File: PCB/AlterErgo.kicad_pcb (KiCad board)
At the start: 2 copper layers, 97 parts, among them J1 GS3, J2 SJ-43514, J3 GS3, SW0:10 SW_Push, SW0:11 SW_Push, SW0:12 SW_Push, SW0:7 SW_Push, SW0:8 SW_Push, SW0:9 SW_Push, SW1 SW_SPST, SW1:10 SW_Push, SW1:11 SW_Push, SW1:12 SW_Push, SW1:13 SW_Push, SW1:9 SW_Push, SW2:10 SW_Push, SW2:11 SW_Push, SW2:12 SW_Push, SW2:13 SW_Push, SW2:7 SW_Push, SW2:8 SW_Push, SW2:9 SW_Push, SW3:10 SW_Push, SW3:11 SW_Push, SW3:12 SW_Push, SW3:13 SW_Push, SW3:8 SW_Push, SW3:9 SW_Push, SW4:10 SW_Push, SW4:11 SW_Push, SW4:12 SW_Push, SW4:13 SW_Push, SW4:7 SW_Push, SW4:8 SW_Push, SW4:9 SW_Push, SW5:10 SW_Push, SW5:11 SW_Push, SW5:12 SW_Push, SW5:13 SW_Push, SW5:7 SW_Push, SW5:8 SW_Push, SW5:9 SW_Push, U1 Feather32u4Bluefruit, U2 MCP23018

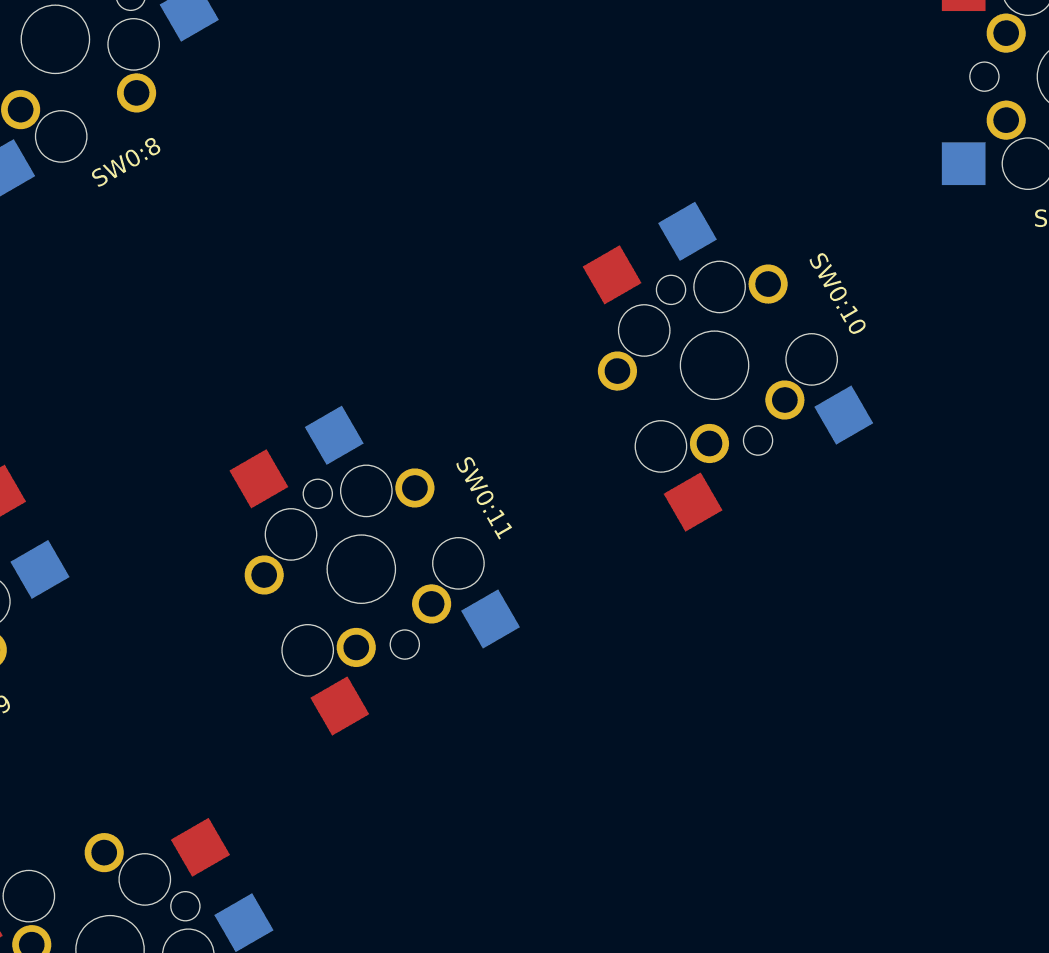
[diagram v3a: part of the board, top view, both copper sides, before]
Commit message: Add stabilizer mounting holes to 2U keys in thumb cluster
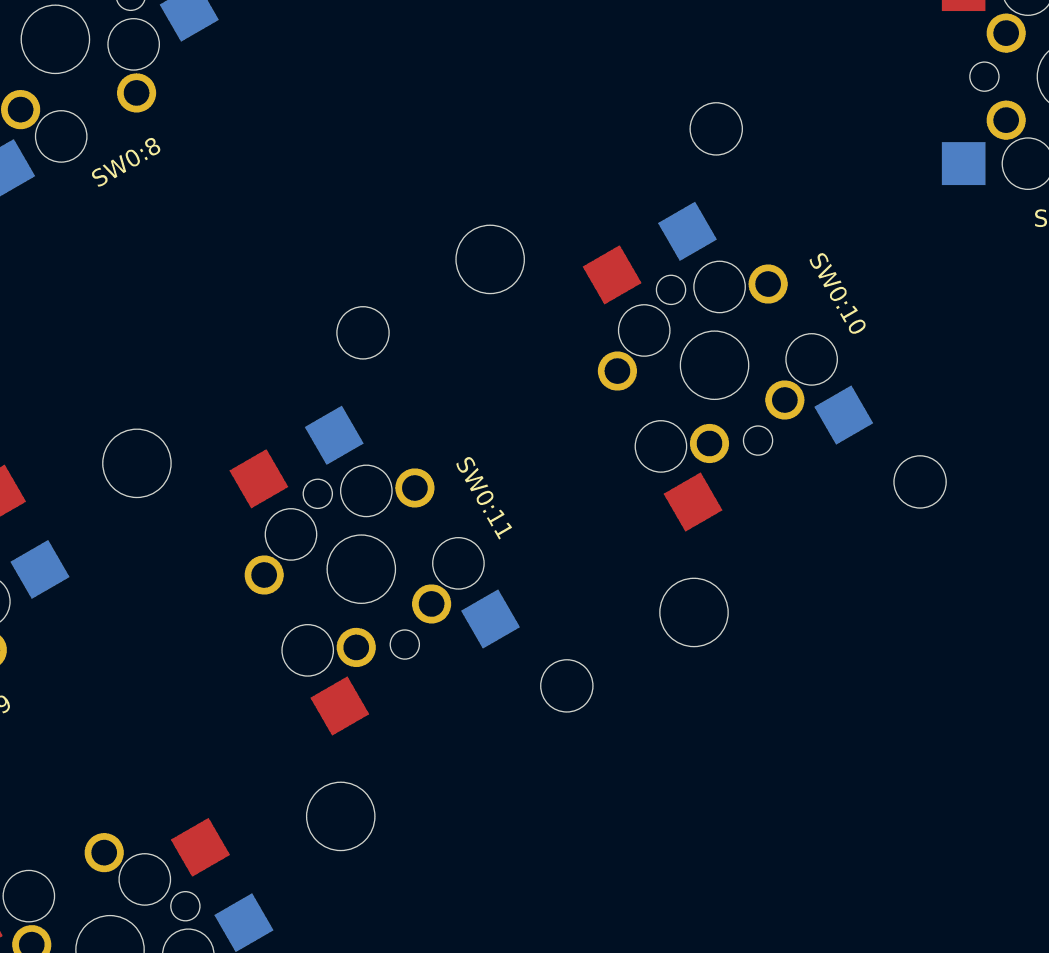
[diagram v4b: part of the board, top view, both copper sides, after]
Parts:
- added SW0:10: SW_Push, keyswitches:Kailh_socket_optional_reversible, F.Cu at (110.1, 168.7)
- added Stab0:11: SW_Stabilizer, keyswitches:MX_Stabilizer_2u, F.Cu at (89.5, 180.6)
- Stab0:10: renamed from SW0:10; value SW_Push -> SW_Stabilizer; footprint keyswitches:Kailh_socket_optional_reversible -> keyswitches:MX_Stabilizer_2u
- turned Stab0:10 to 300 degrees
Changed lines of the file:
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@@
     (links 388)
     (no_connects 388)
-    (area 40.508856 -74.833 449.550001 213.296599)
+    (area 40.556456 -74.7854 449.502401 213.248999)
     (thickness 1.6)
     (drawings 11)
     (tracks 0)
     (zones 0)
-    (modules 97)
+    (modules 99)
     (nets 83)
   )
@@
   )
   (module keyswitches:Kailh_socket_optional_reversible (layer F.Cu)
+    (at 110.132883 168.652792 120)
+    (descr "MX-style keyswitch with support for reversible optional Kailh socket")
+    (tags MX,cherry,gateron,kailh,pg1511,socket)
+    (fp_text reference SW0:10 (at 0 8.3 120) (layer F.SilkS)
+      (effects (font (size 1 1) (thickness 0.15)))
+    )
+    (fp_text value SW_Push (at 0 -8.7 120) (layer F.Fab)
+      (effects (font (size 1 1) (thickness 0.15)))
+    )
+    (fp_line (start -7 -6) (end -7 -7) (layer B.SilkS) (width 0.15))
+    (fp_line (start -7 -7) (end -6 -7) (layer B.SilkS) (width 0.15))
+    (fp_line (start -6 7) (end -7 7) (layer B.SilkS) (width 0.15))
+    (fp_line (start -7 7) (end -7 6) (layer B.SilkS) (width 0.15))
+    (fp_line (start 7 6) (end 7 7) (layer B.SilkS) (width 0.15))
+    (fp_line (start 7 7) (end 6 7) (layer B.SilkS) (width 0.15))
+    (fp_line (start 6 -7) (end 7 -7) (layer B.SilkS) (width 0.15))
+    (fp_line (start 7 -7) (end 7 -6) (layer B.SilkS) (width 0.15))
+    (fp_line (start -6.9 6.9) (end 6.9 6.9) (layer Eco2.User) (width 0.15))
+    (fp_line (start 6.9 -6.9) (end -6.9 -6.9) (layer Eco2.User) (width 0.15))
+    (fp_line (start 6.9 -6.9) (end 6.9 6.9) (layer Eco2.User) (width 0.15))
+    (fp_line (start -6.9 6.9) (end -6.9 -6.9) (layer Eco2.User) (width 0.15))
+    (fp_line (start -7.5 -7.5) (end 7.5 -7.5) (layer Eco2.User) (width 0.15))
+    (fp_line (start 7.5 -7.5) (end 7.5 7.5) (layer Eco2.User) (width 0.15))
+    (fp_line (start 7.5 7.5) (end -7.5 7.5) (layer Eco2.User) (width 0.15))
+    (fp_line (start -7.5 7.5) (end -7.5 -7.5) (layer Eco2.User) (width 0.15))
+    (pad 1 smd rect (at -6.29 5.08 120) (size 2.55 2.5) (layers B.Cu B.Paste B.Mask)
+      (net 60 /ROW0))
+    (pad 2 smd rect (at 7.56 2.54 120) (size 2.55 2.5) (layers B.Cu B.Paste B.Mask)
+      (net 8 "Net-(D0:10-Pad2)"))
+    (pad "" np_thru_hole circle (at -2.54 -5.08 120) (size 3 3) (drill 3) (layers *.Cu *.Mask))
+    (pad "" np_thru_hole circle (at 3.81 -2.54 120) (size 3 3) (drill 3) (layers *.Cu *.Mask))
+    (pad 2 thru_hole circle (at 2.54 5.08 120) (size 2.286 2.286) (drill 1.4986) (layers *.Cu *.Mask)
+      (net 8 "Net-(D0:10-Pad2)"))
+    (pad 1 thru_hole circle (at -3.81 2.54 120) (size 2.286 2.286) (drill 1.4986) (layers *.Cu *.Mask)
+      (net 60 /ROW0))
+    (pad 1 smd rect (at -6.29 -5.08 120) (size 2.55 2.5) (layers F.Cu F.Paste F.Mask)
+      (net 60 /ROW0))
+    (pad "" np_thru_hole circle (at -2.54 5.08 120) (size 3 3) (drill 3) (layers *.Cu *.Mask))
+    (pad "" np_thru_hole circle (at 3.81 2.54 120) (size 3 3) (drill 3) (layers *.Cu *.Mask))
+    (pad 2 thru_hole circle (at 2.54 -5.08 120) (size 2.286 2.286) (drill 1.4986) (layers *.Cu *.Mask)
+      (net 8 "Net-(D0:10-Pad2)"))
+    (pad "" np_thru_hole circle (at 0 0 120) (size 3.9878 3.9878) (drill 3.9878) (layers *.Cu *.Mask))
+    (pad 1 thru_hole circle (at -3.81 -2.54 120) (size 2.286 2.286) (drill 1.4986) (layers *.Cu *.Mask)
+      (net 60 /ROW0))
+    (pad "" np_thru_hole circle (at 5.08 0 120) (size 1.7018 1.7018) (drill 1.7018) (layers *.Cu *.Mask))
+    (pad "" np_thru_hole circle (at -5.08 0 120) (size 1.7018 1.7018) (drill 1.7018) (layers *.Cu *.Mask))
+    (pad 2 smd rect (at 7.56 -2.54 120) (size 2.55 2.5) (layers F.Cu F.Paste F.Mask)
+      (net 8 "Net-(D0:10-Pad2)"))
+  )
+  (module keyswitches:Kailh_socket_optional_reversible (layer F.Cu)
     (at 107.15628 107.1563)
     (descr "MX-style keyswitch with support for reversible optional Kailh socket")
@@
   )
   (module keyswitches:Kailh_socket_optional_reversible (layer F.Cu)
-    (at 110.132883 168.652792 120)
-    (descr "MX-style keyswitch with support for reversible optional Kailh socket")
-    (tags MX,cherry,gateron,kailh,pg1511,socket)
-    (fp_text reference SW0:10 (at 0 8.3 120) (layer F.SilkS)
-      (effects (font (size 1 1) (thickness 0.15)))
-    )
-    (fp_text value SW_Push (at 0 -8.7 120) (layer F.Fab)
-      (effects (font (size 1 1) (thickness 0.15)))
-    )
-    (fp_line (start -7 -6) (end -7 -7) (layer B.SilkS) (width 0.15))
-    (fp_line (start -7 -7) (end -6 -7) (layer B.SilkS) (width 0.15))
-    (fp_line (start -6 7) (end -7 7) (layer B.SilkS) (width 0.15))
-    (fp_line (start -7 7) (end -7 6) (layer B.SilkS) (width 0.15))
-    (fp_line (start 7 6) (end 7 7) (layer B.SilkS) (width 0.15))
-    (fp_line (start 7 7) (end 6 7) (layer B.SilkS) (width 0.15))
-    (fp_line (start 6 -7) (end 7 -7) (layer B.SilkS) (width 0.15))
-    (fp_line (start 7 -7) (end 7 -6) (layer B.SilkS) (width 0.15))
-    (fp_line (start -6.9 6.9) (end 6.9 6.9) (layer Eco2.User) (width 0.15))
-    (fp_line (start 6.9 -6.9) (end -6.9 -6.9) (layer Eco2.User) (width 0.15))
-    (fp_line (start 6.9 -6.9) (end 6.9 6.9) (layer Eco2.User) (width 0.15))
-    (fp_line (start -6.9 6.9) (end -6.9 -6.9) (layer Eco2.User) (width 0.15))
-    (fp_line (start -7.5 -7.5) (end 7.5 -7.5) (layer Eco2.User) (width 0.15))
-    (fp_line (start 7.5 -7.5) (end 7.5 7.5) (layer Eco2.User) (width 0.15))
-    (fp_line (start 7.5 7.5) (end -7.5 7.5) (layer Eco2.User) (width 0.15))
-    (fp_line (start -7.5 7.5) (end -7.5 -7.5) (layer Eco2.User) (width 0.15))
-    (pad 1 smd rect (at -6.29 5.08 120) (size 2.55 2.5) (layers B.Cu B.Paste B.Mask)
-      (net 60 /ROW0))
-    (pad 2 smd rect (at 7.56 2.54 120) (size 2.55 2.5) (layers B.Cu B.Paste B.Mask)
-      (net 8 "Net-(D0:10-Pad2)"))
-    (pad "" np_thru_hole circle (at -2.54 -5.08 120) (size 3 3) (drill 3) (layers *.Cu *.Mask))
-    (pad "" np_thru_hole circle (at 3.81 -2.54 120) (size 3 3) (drill 3) (layers *.Cu *.Mask))
-    (pad 2 thru_hole circle (at 2.54 5.08 120) (size 2.286 2.286) (drill 1.4986) (layers *.Cu *.Mask)
-      (net 8 "Net-(D0:10-Pad2)"))
-    (pad 1 thru_hole circle (at -3.81 2.54 120) (size 2.286 2.286) (drill 1.4986) (layers *.Cu *.Mask)
-      (net 60 /ROW0))
-    (pad 1 smd rect (at -6.29 -5.08 120) (size 2.55 2.5) (layers F.Cu F.Paste F.Mask)
-      (net 60 /ROW0))
-    (pad "" np_thru_hole circle (at -2.54 5.08 120) (size 3 3) (drill 3) (layers *.Cu *.Mask))
-    (pad "" np_thru_hole circle (at 3.81 2.54 120) (size 3 3) (drill 3) (layers *.Cu *.Mask))
-    (pad 2 thru_hole circle (at 2.54 -5.08 120) (size 2.286 2.286) (drill 1.4986) (layers *.Cu *.Mask)
-      (net 8 "Net-(D0:10-Pad2)"))
-    (pad "" np_thru_hole circle (at 0 0 120) (size 3.9878 3.9878) (drill 3.9878) (layers *.Cu *.Mask))
-    (pad 1 thru_hole circle (at -3.81 -2.54 120) (size 2.286 2.286) (drill 1.4986) (layers *.Cu *.Mask)
-      (net 60 /ROW0))
-    (pad "" np_thru_hole circle (at 5.08 0 120) (size 1.7018 1.7018) (drill 1.7018) (layers *.Cu *.Mask))
-    (pad "" np_thru_hole circle (at -5.08 0 120) (size 1.7018 1.7018) (drill 1.7018) (layers *.Cu *.Mask))
-    (pad 2 smd rect (at 7.56 -2.54 120) (size 2.55 2.5) (layers F.Cu F.Paste F.Mask)
-      (net 8 "Net-(D0:10-Pad2)"))
-  )
-  (module keyswitches:Kailh_socket_optional_reversible (layer F.Cu)
     (at 89.510653 180.559042 120)
     (descr "MX-style keyswitch with support for reversible optional Kailh socket")
@@
     (pad "" np_thru_hole circle (at -5.08 0 90) (size 1.7018 1.7018) (drill 1.7018) (layers *.Cu *.Mask))
   )
+  (module keyswitches:MX_Stabilizer_2u (layer F.Cu)
+    (at 89.510653 180.559042 300)
+    (descr "MX-style stabilizer mount")
+    (tags MX,cherry,gateron,kailh,pg1511,stabilizer,stab)
+    (fp_text reference Stab0:11 (at 0 10 300) (layer Cmts.User) hide
+      (effects (font (size 1 1) (thickness 0.15)))
+    )
+    (fp_text value SW_Stabilizer (at 0 -8.7 300) (layer F.Fab) hide
+      (effects (font (size 1 1) (thickness 0.15)))
+    )
+    (fp_circle (center 0 0) (end 3 0) (layer Cmts.User) (width 0.15))
+    (pad "" np_thru_hole circle (at -11.9 -6.985 300) (size 3.048 3.048) (drill 3.048) (layers *.Cu *.Mask))
+    (pad "" np_thru_hole circle (at 11.9 -6.985 300) (size 3.048 3.048) (drill 3.048) (layers *.Cu *.Mask))
+    (pad "" np_thru_hole circle (at -11.9 8.255 300) (size 3.9878 3.9878) (drill 3.9878) (layers *.Cu *.Mask))
+    (pad "" np_thru_hole circle (at 11.9 8.255 300) (size 3.9878 3.9878) (drill 3.9878) (layers *.Cu *.Mask))
+  )
+  (module keyswitches:MX_Stabilizer_2u (layer F.Cu)
+    (at 110.132883 168.652792 300)
+    (descr "MX-style stabilizer mount")
+    (tags MX,cherry,gateron,kailh,pg1511,stabilizer,stab)
+    (fp_text reference Stab0:10 (at 0 10 300) (layer Cmts.User) hide
+      (effects (font (size 1 1) (thickness 0.15)))
+    )
+    (fp_text value SW_Stabilizer (at 0 -8.7 300) (layer F.Fab) hide
+      (effects (font (size 1 1) (thickness 0.15)))
+    )
+    (fp_circle (center 0 0) (end 3 0) (layer Cmts.User) (width 0.15))
+    (pad "" np_thru_hole circle (at -11.9 -6.985 300) (size 3.048 3.048) (drill 3.048) (layers *.Cu *.Mask))
+    (pad "" np_thru_hole circle (at 11.9 -6.985 300) (size 3.048 3.048) (drill 3.048) (layers *.Cu *.Mask))
+    (pad "" np_thru_hole circle (at -11.9 8.255 300) (size 3.9878 3.9878) (drill 3.9878) (layers *.Cu *.Mask))
+    (pad "" np_thru_hole circle (at 11.9 8.255 300) (size 3.9878 3.9878) (drill 3.9878) (layers *.Cu *.Mask))
+  )
   (dimension 23.8125 (width 0.3) (layer Eco2.User)
